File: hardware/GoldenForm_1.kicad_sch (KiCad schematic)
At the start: 41 parts, among them IC1 UVLO, J1 Conn_01x02_Pin, J2 1140084168, J3 Conn_01x04_Pin, J4 USB4105-GF-A, M3 MountingHole x 4, U2 BNO055, U3 Buck_Boost, U4 ESP32-S3-WROOM-1

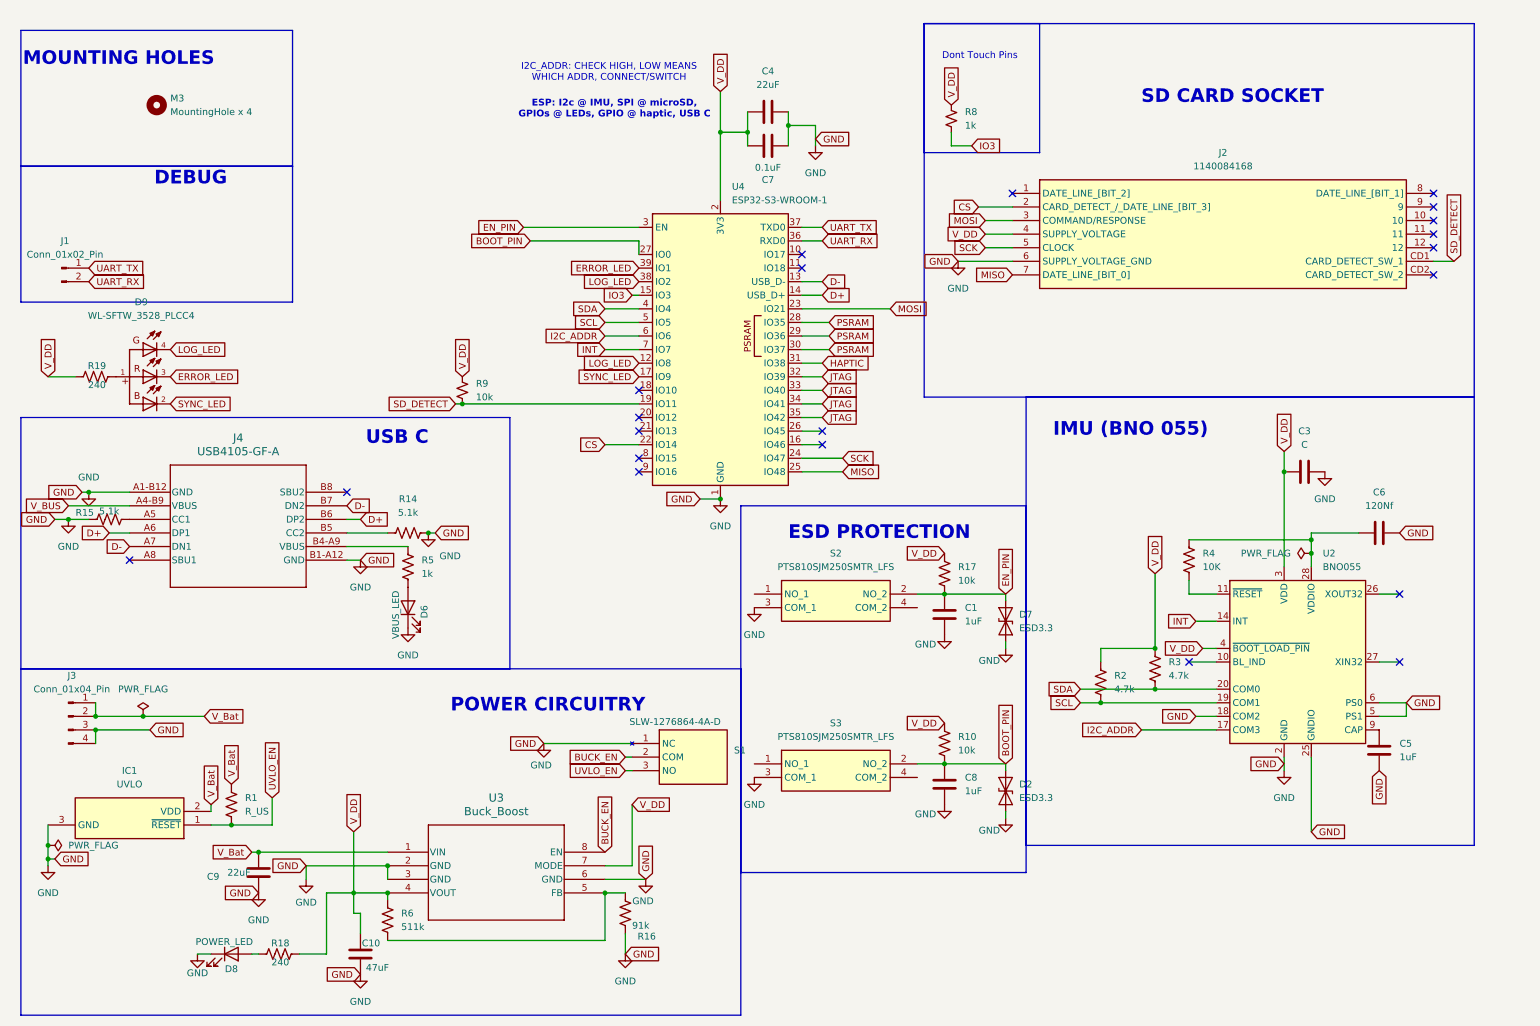
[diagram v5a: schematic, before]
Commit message: placed the components on the PCB
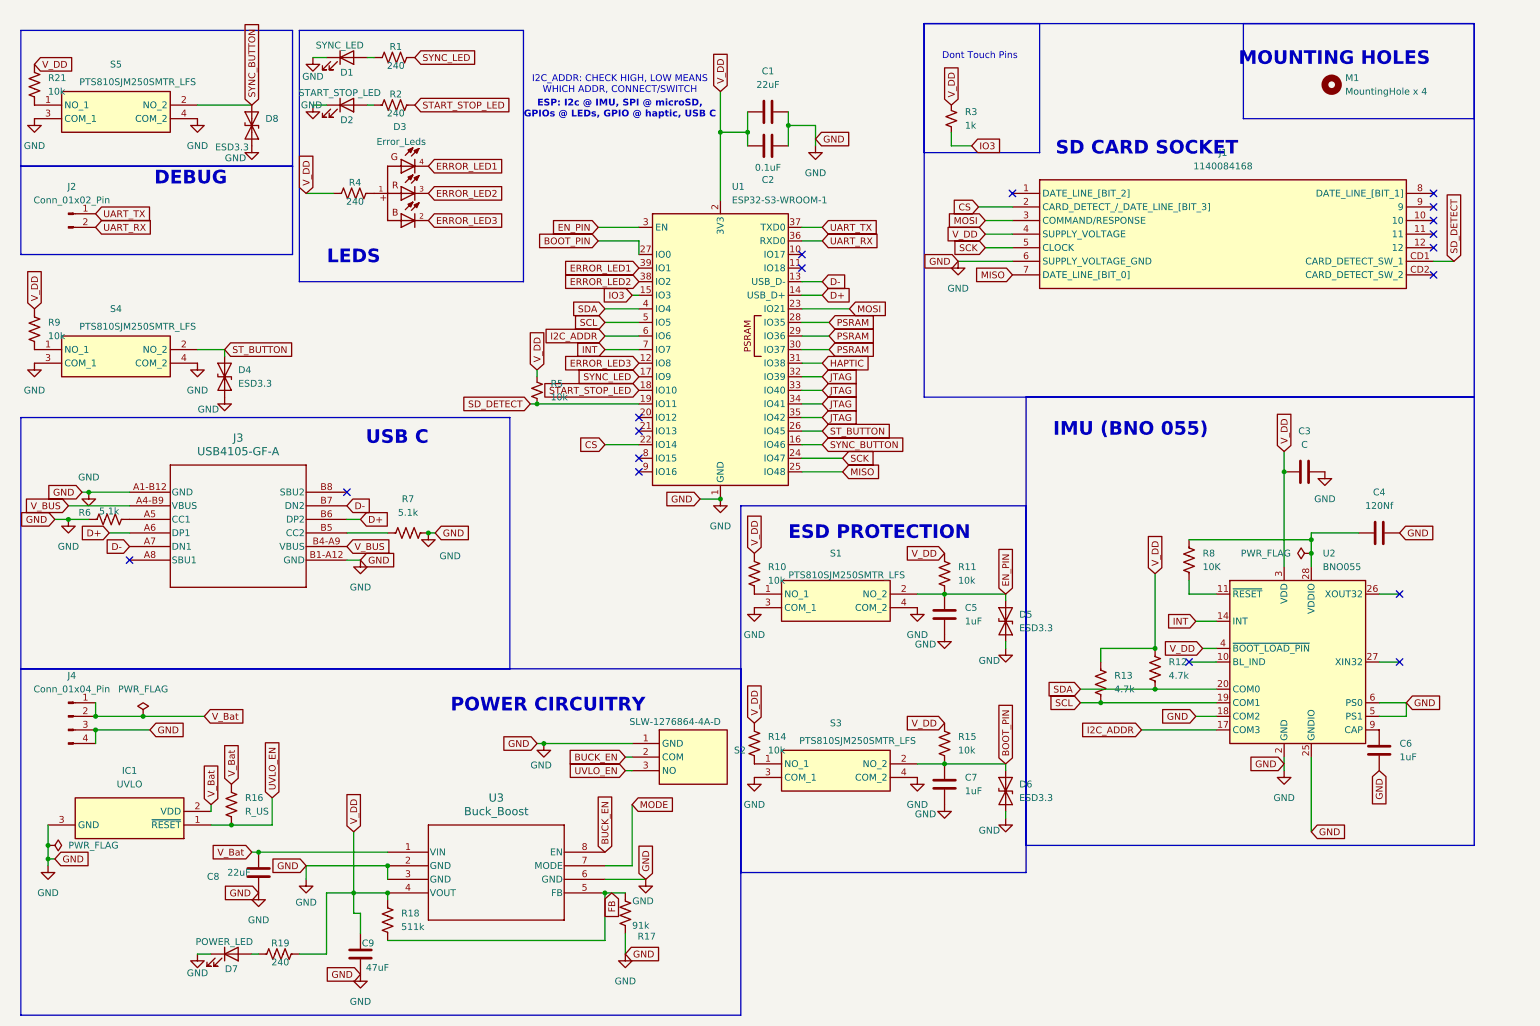
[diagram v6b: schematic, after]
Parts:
- removed D6: VBUS_LED, symbol Device:LED
- removed R5: 1k, symbol Device:R_US
- added D1: SYNC_LED, LED_SMD:LED_0805_2012Metric_Pad1.15x1.40mm_HandSolder, symbol Device:LED
- added D2: START_STOP_LED, LED_SMD:LED_0805_2012Metric_Pad1.15x1.40mm_HandSolder, symbol Device:LED
- added D4, D8: ESD3.3, Diode_SMD:D_SOD-923, symbol Diode:ESD9B3.3ST5G
- added R1, R2: 240, Resistor_SMD:R_0805_2012Metric_Pad1.20x1.40mm_HandSolder, symbol Device:R_US
- added R10, R14, R21, R9: 10k, Resistor_SMD:R_0805_2012Metric_Pad1.20x1.40mm_HandSolder, symbol Device:R_US
- added S4, S5: PTS810SJM250SMTR_LFS, MyFootprints:PTS810SJM250SMTRLFS, symbol MySymbols:PTS810SJM250SMTR_LFS
- C1: renamed from C4; footprint (none) -> Capacitor_SMD:C_0805_2012Metric_Pad1.18x1.45mm_HandSolder
- C2: renamed from C7; footprint (none) -> Capacitor_SMD:C_0805_2012Metric_Pad1.18x1.45mm_HandSolder
- C5: renamed from C1; footprint (none) -> Capacitor_SMD:C_0805_2012Metric_Pad1.18x1.45mm_HandSolder
- C7: renamed from C8; footprint (none) -> Capacitor_SMD:C_0805_2012Metric_Pad1.18x1.45mm_HandSolder
- C8: renamed from C9; footprint (none) -> Capacitor_SMD:C_0603_1608Metric_Pad1.08x0.95mm_HandSolder
- C9: renamed from C10; footprint (none) -> Capacitor_SMD:C_0603_1608Metric_Pad1.08x0.95mm_HandSolder
- D3: renamed from D9; value WL-SFTW_3528_PLCC4 -> Error_Leds
- D7: renamed from D8; footprint (none) -> LED_SMD:LED_0805_2012Metric_Pad1.15x1.40mm_HandSolder
- R11: renamed from R17; footprint (none) -> Resistor_SMD:R_0805_2012Metric_Pad1.20x1.40mm_HandSolder
- R12: renamed from R3; footprint (none) -> Resistor_SMD:R_0805_2012Metric_Pad1.20x1.40mm_HandSolder
- R13: renamed from R2; footprint (none) -> Resistor_SMD:R_0805_2012Metric_Pad1.20x1.40mm_HandSolder
- R15: renamed from R10; footprint (none) -> Resistor_SMD:R_0805_2012Metric_Pad1.20x1.40mm_HandSolder
- R17: renamed from R16; footprint (none) -> Resistor_SMD:R_0805_2012Metric_Pad1.20x1.40mm_HandSolder
- R18: renamed from R6; footprint (none) -> Resistor_SMD:R_0805_2012Metric_Pad1.20x1.40mm_HandSolder
- R19: renamed from R18; footprint (none) -> Resistor_SMD:R_0805_2012Metric_Pad1.20x1.40mm_HandSolder
- R3: renamed from R8; footprint (none) -> Resistor_SMD:R_0805_2012Metric_Pad1.20x1.40mm_HandSolder
- R4: renamed from R19; footprint (none) -> Resistor_SMD:R_0805_2012Metric_Pad1.20x1.40mm_HandSolder
- R5: renamed from R9; footprint (none) -> Resistor_SMD:R_0805_2012Metric_Pad1.20x1.40mm_HandSolder
- R6: renamed from R15; footprint (none) -> Resistor_SMD:R_0805_2012Metric_Pad1.20x1.40mm_HandSolder
- R7: renamed from R14; footprint (none) -> Resistor_SMD:R_0805_2012Metric_Pad1.20x1.40mm_HandSolder
- R8: renamed from R4; footprint (none) -> Resistor_SMD:R_0805_2012Metric_Pad1.20x1.40mm_HandSolder
- renumbered C6 to C4, C5 to C6, D7 to D5, D2 to D6, J2 to J1, J1 to J2, J4 to J3, J3 to J4, M3 to M1, R1 to R16, S2 to S1, S1 to S2, U4 to U1
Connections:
- net GND: now also S1.4 (COM_2), S3.4 (COM_2), D1.1 (K), D2.1 (K), D4.1 (A1), D8.1 (A1), S4.3 (COM_1), S4.4 (COM_2), S5.3 (COM_1), S5.4 (COM_2)
- net SYNC_LED: now also R1.2; no longer D3.2
- net V_BUS: now also J3.B4-A9 (VBUS)
- net V_DD: now also R10.1, R14.1, R21.1, R9.1; no longer U3.7 (MODE)
- net at S1.1 (NO_1): now also R10.2
- net FB: now reaches R17.1, R18.2, U3.5 (FB)
- net at S3.1 (NO_1): now also R14.2
- net SYNC_BUTTON: now reaches U1.16 (IO46)
- net SYNC_BUTTON: now also D8.2 (A2), S5.2 (NO_2)
- net START_STOP_LED: now reaches U1.18 (IO10)
- net START_STOP_LED: now also R2.2
- net ST_BUTTON: now reaches U1.26 (IO45)
- net ST_BUTTON: now also D4.2 (A2), S4.2 (NO_2)
- net ERROR_LED renamed ERROR_LED1
- net ERROR_LED1: now also D3.4; no longer D3.3
- removed net LOG_LED: D3.4, U1.12 (IO8), U1.38 (IO2)
- new net: D2.2 (A), R2.1
- new net: R21.2, S5.1 (NO_1)
- new net: D1.2 (A), R1.1
- new net: R9.2, S4.1 (NO_1)
- new net ERROR_LED2: D3.3, U1.38 (IO2)
- new net ERROR_LED3: D3.2, U1.12 (IO8)
- new net MODE: U3.7 (MODE)
- no-connect marks 21 -> 18
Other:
- note added: "LEDS"
- moved on the sheet: D3, J2, M1, R4, R5

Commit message: added transistor and haptic onto board
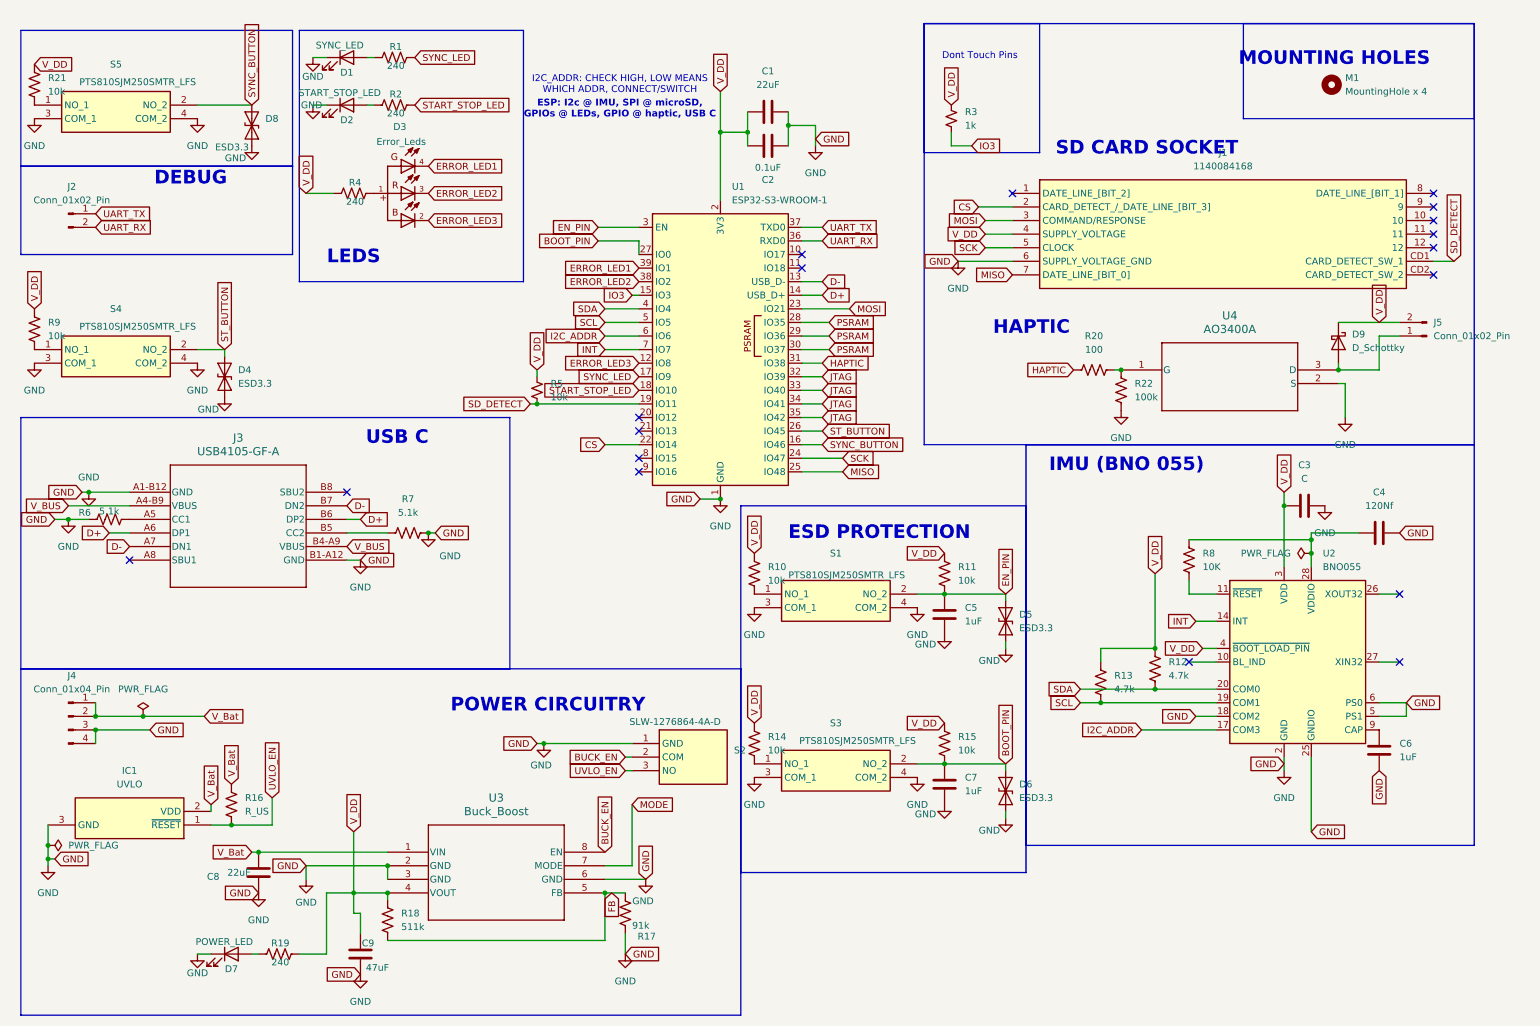
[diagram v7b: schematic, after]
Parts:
- added D9: D_Schottky, Diode_SMD:D_SOD-323_HandSoldering, symbol Device:D_Schottky
- added J5: Conn_01x02_Pin, Connector_PinHeader_1.00mm:PinHeader_1x02_P1.00mm_Vertical, symbol Connector:Conn_01x02_Pin
- added R20: 100, Resistor_SMD:R_0805_2012Metric_Pad1.20x1.40mm_HandSolder, symbol Device:R_US
- added R22: 100k, Resistor_SMD:R_0805_2012Metric_Pad1.20x1.40mm_HandSolder, symbol Device:R_US
- added U4: AO3400A, MyFootprints:SOT-23-3L_AOS, symbol MySymbols:AO3400A
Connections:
- net GND: now also R22.1, U4.2 (S)
- net HAPTIC: now also R20.1
- net V_DD: now also D9.1 (K), J5.2 (Pin_2)
- new net: R20.2, R22.2, U4.1 (G)
- new net: D9.2 (A), J5.1 (Pin_1), U4.3 (D)
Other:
- note added: "HAPTIC"
- moved on the sheet: C3

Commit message: started routing. added classes and stuff
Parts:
- C3: value C -> 100nF
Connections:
- net ERROR_LED1: now also U1.38 (IO2); no longer U1.39 (IO1)
- net ERROR_LED2: now also U1.39 (IO1); no longer U1.38 (IO2)
- net ST_BUTTON: now also U1.10 (IO17); no longer U1.26 (IO45)
- net SYNC_BUTTON: now also U1.11 (IO18); no longer U1.16 (IO46)
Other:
- note added: "USER SWITCHES"
- moved on the sheet: D4, D8, J2, R21, R9, S4, S5
